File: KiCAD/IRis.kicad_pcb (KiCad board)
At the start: 2 copper layers, 31.3 x 31.3 mm, 25 parts, among them P1 Digital Out, Q1 MMBF4117, Q2 MMBF4117, Q3 MMBF4117, U1 TSV911ILT, U2 TLV3201

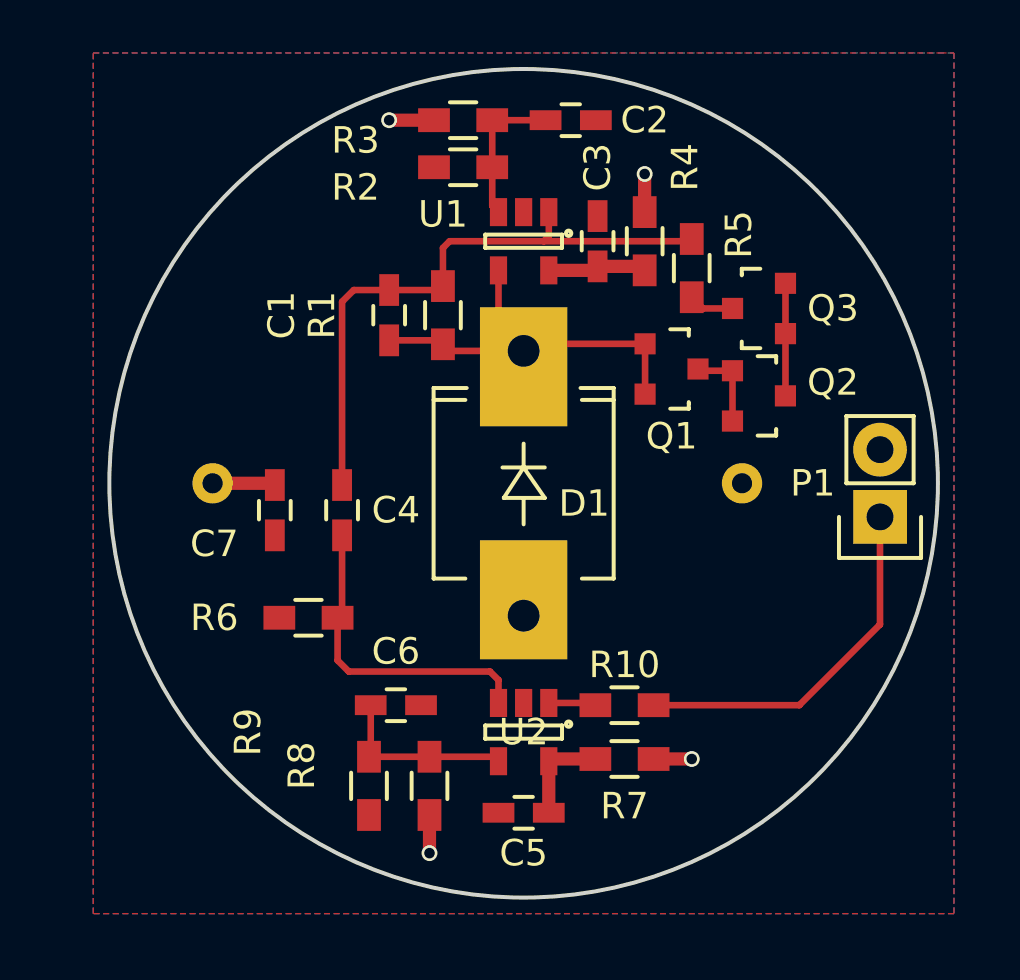
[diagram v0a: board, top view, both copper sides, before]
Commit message: Added negative voltage input protection to comparator U2; fixed copper fill clearances for OSHPark
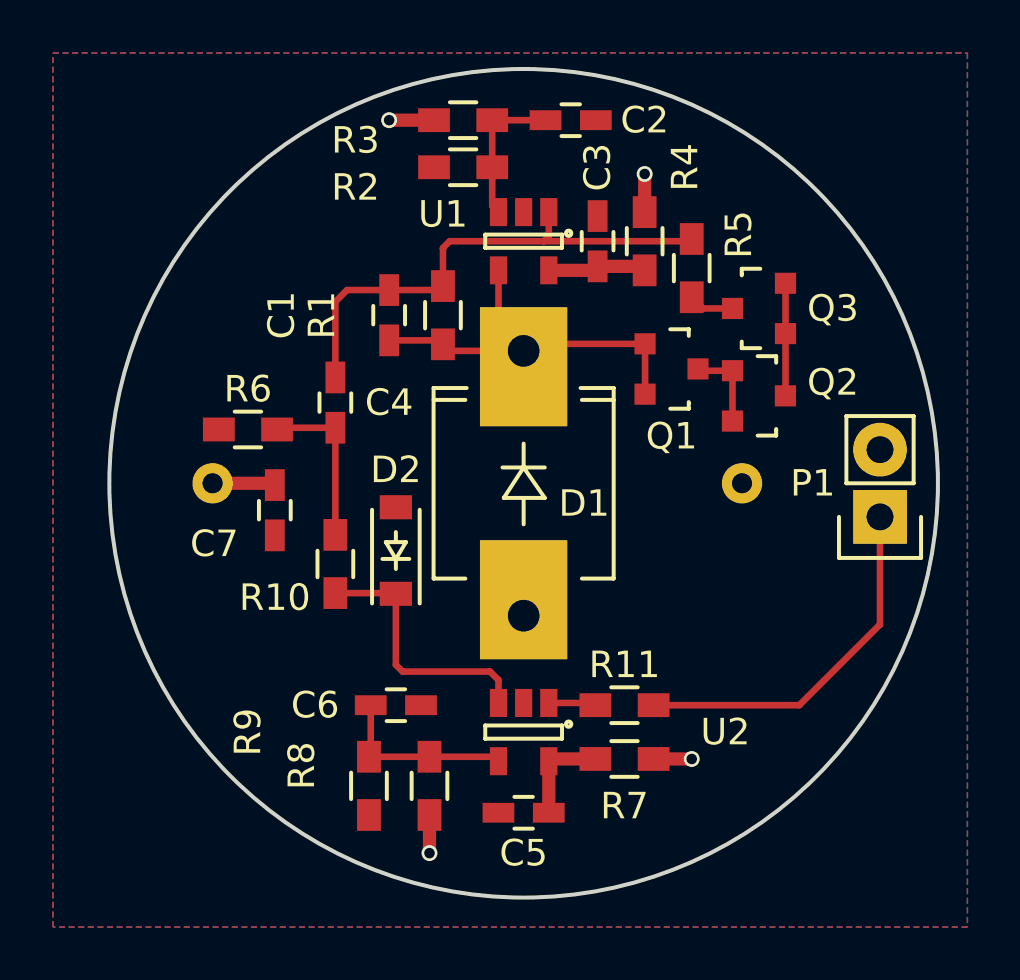
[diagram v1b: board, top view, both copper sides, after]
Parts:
- added D2: MBR0520, Diodes_SMD:SOD-123, F.Cu at (137.4, 102.1)
- added R11: 100, Resistors_SMD:R_0603_HandSoldering, F.Cu at (146.1, 108.0)
- D1: value PD70-01C/TR7 -> VBPW34FASR
- R10: value 100 -> 5.1k
- R6: value 10k -> 5.1k
- moved R10 12.2 mm to (135.1, 102.6), turned to 270 degrees
- moved R6 7.47 mm to (131.8, 97.5)
- moved C4 4.07 mm to (135.1, 96.5)
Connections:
- R10 pad 1: Net-(R10-Pad1) -> Net-(C4-Pad1)
- R10 pad 2: Net-(P1-Pad1) -> Net-(D2-Pad1)
- U2 pad 1: Net-(R10-Pad1) -> Net-(R11-Pad1)
- U2 pad 3: Net-(C4-Pad1) -> Net-(D2-Pad1)
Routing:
- net Net-(D2-Pad1): track 0.00 -> 9.96 mm
- net Net-(C4-Pad1): track 12.0 -> 6.28 mm
- net Net-(C1-Pad1): track 23.5 -> 19.6 mm
- net Net-(R11-Pad1): track 0.00 -> 2.03 mm
- net Net-(R10-Pad1): track 1.91 -> 0.00 mm

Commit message: Updated board and Gerbers to v1.4
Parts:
- moved R11 4.06 mm to (150.1, 108.0)
- moved R6 1.44 mm to (132.8, 96.5), turned to 270 degrees
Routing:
- net Net-(R11-Pad1): track 2.03 -> 5.98 mm
- net Net-(P1-Pad1): track 13.9 -> 9.96 mm
- net +5V: track 8.58 -> 10.1 mm
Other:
- board text added: "IRis v1.4"
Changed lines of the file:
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@@
     (links 48)
     (no_connects 0)
-    (area 124.46 82.827 160.048429 116.332001)
+    (area 126.51563 83.84363 157.96437 115.29237)
     (thickness 1.6)
-    (drawings 1)
-    (tracks 78)
+    (drawings 2)
+    (tracks 81)
     (zones 0)
     (modules 27)
@@
   )
   (setup
-    (last_trace_width 0.25)
+    (last_trace_width 0.5)
     (user_trace_width 0.5)
     (trace_clearance 0.2)
@@
     (tags "capacitor 0603")
     (attr smd)
-    (fp_text reference C1 (at 0 4.064 270) (layer F.SilkS)
+    (fp_text reference C1 (at -0.762 4.572 270) (layer F.SilkS)
       (effects (font (size 1 1) (thickness 0.15)))
     )
@@
     (tags "capacitor 0603")
     (attr smd)
-    (fp_text reference C4 (at 0 2.032 180) (layer F.SilkS)
+    (fp_text reference C4 (at 0 1.524 270) (layer F.SilkS)
       (effects (font (size 1 1) (thickness 0.15)))
     )
@@
     (tags "resistor 0603")
     (attr smd)
-    (fp_text reference R1 (at 0 4.572 270) (layer F.SilkS)
+    (fp_text reference R1 (at -0.762 5.334 270) (layer F.SilkS)
       (effects (font (size 1 1) (thickness 0.15)))
     )
@@
   )
   (module Resistors_SMD:R_0603_HandSoldering (layer F.Cu)
-    (at 131.826 97.536)
-    (descr "Resistor SMD 0603, hand soldering")
-    (tags "resistor 0603")
-    (attr smd)
-    (fp_text reference R6 (at 0 -1.524) (layer F.SilkS)
-      (effects (font (size 1 1) (thickness 0.15)))
-    )
-    (fp_text value 5.1k (at 0 1.9) (layer F.Fab)
-      (effects (font (size 1 1) (thickness 0.15)))
-    )
-    (fp_line (start -2 -0.8) (end 2 -0.8) (layer F.CrtYd) (width 0.05))
-    (fp_line (start -2 0.8) (end 2 0.8) (layer F.CrtYd) (width 0.05))
-    (fp_line (start -2 -0.8) (end -2 0.8) (layer F.CrtYd) (width 0.05))
-    (fp_line (start 2 -0.8) (end 2 0.8) (layer F.CrtYd) (width 0.05))
-    (fp_line (start 0.5 0.675) (end -0.5 0.675) (layer F.SilkS) (width 0.15))
-    (fp_line (start -0.5 -0.675) (end 0.5 -0.675) (layer F.SilkS) (width 0.15))
-    (pad 1 smd rect (at -1.1 0) (size 1.2 0.9) (layers F.Cu F.Paste F.Mask)
-      (net 4 GND))
-    (pad 2 smd rect (at 1.1 0) (size 1.2 0.9) (layers F.Cu F.Paste F.Mask)
+    (at 132.842 96.52 270)
+    (descr "Resistor SMD 0603, hand soldering")
+    (tags "resistor 0603")
+    (attr smd)
+    (fp_text reference R6 (at 0 1.524 270) (layer F.SilkS)
+      (effects (font (size 1 1) (thickness 0.15)))
+    )
+    (fp_text value 5.1k (at 0 1.9 270) (layer F.Fab)
+      (effects (font (size 1 1) (thickness 0.15)))
+    )
+    (fp_line (start -2 -0.8) (end 2 -0.8) (layer F.CrtYd) (width 0.05))
+    (fp_line (start -2 0.8) (end 2 0.8) (layer F.CrtYd) (width 0.05))
+    (fp_line (start -2 -0.8) (end -2 0.8) (layer F.CrtYd) (width 0.05))
+    (fp_line (start 2 -0.8) (end 2 0.8) (layer F.CrtYd) (width 0.05))
+    (fp_line (start 0.5 0.675) (end -0.5 0.675) (layer F.SilkS) (width 0.15))
+    (fp_line (start -0.5 -0.675) (end 0.5 -0.675) (layer F.SilkS) (width 0.15))
+    (pad 1 smd rect (at -1.1 0 270) (size 1.2 0.9) (layers F.Cu F.Paste F.Mask)
+      (net 4 GND))
+    (pad 2 smd rect (at 1.1 0 270) (size 1.2 0.9) (layers F.Cu F.Paste F.Mask)
       (net 6 "Net-(C4-Pad1)"))
     (model Resistors_SMD.3dshapes/R_0603_HandSoldering.wrl
@@
     (tags SOT-23-5)
     (attr smd)
-    (fp_text reference U2 (at 0 -7.62 360) (layer F.SilkS)
+    (fp_text reference U2 (at -1.016 -2.794 360) (layer F.SilkS)
       (effects (font (size 1 1) (thickness 0.15)))
     )
@@
   )
   (module Resistors_SMD:R_0603_HandSoldering (layer F.Cu)
-    (at 146.05 107.95)
+    (at 150.114 107.95)
     (descr "Resistor SMD 0603, hand soldering")
     (tags "resistor 0603")
@@
       (rotate (xyz 0 0 0))
     )
+  )
+  (gr_text "IRis v1.4" (at 149.606 102.616) (layer F.SilkS)
+    (effects (font (size 1 1) (thickness 0.25)))
   )
   (gr_circle (center 142.24 99.568) (end 154.94 108.712) (layer Edge.Cuts) (width 0.15))
@@
   (segment (start 144.884 91.524) (end 145.034 91.374) (width 0.5) (layer F.Cu) (net 5))
   (segment (start 143.34 91.374) (end 143.19 91.524) (width 0.25) (layer F.Cu) (net 5))
+  (segment (start 135.128 97.47) (end 132.992 97.47) (width 0.25) (layer F.Cu) (net 6))
+  (segment (start 132.992 97.47) (end 132.842 97.62) (width 0.25) (layer F.Cu) (net 6))
   (segment (start 135.128 97.47) (end 135.128 101.516) (width 0.25) (layer F.Cu) (net 6))
-  (segment (start 135.128 97.47) (end 132.992 97.47) (width 0.25) (layer F.Cu) (net 6))
-  (segment (start 132.992 97.47) (end 132.926 97.536) (width 0.25) (layer F.Cu) (net 6))
   (segment (start 143.19 110.066) (end 143.19 112.014) (width 0.5) (layer F.Cu) (net 7))
   (segment (start 144.95 109.982) (end 143.274 109.982) (width 0.5) (layer F.Cu) (net 7))
@@
   (segment (start 136.464 107.95) (end 136.464 109.832) (width 0.25) (layer F.Cu) (net 8))
   (segment (start 136.464 109.832) (end 136.398 109.898) (width 0.25) (layer F.Cu) (net 8))
+  (segment (start 138.854 85.852) (end 137.668 85.852) (width 0.5) (layer F.Cu) (net 9))
+  (via (at 137.414 86.868) (size 0.6) (drill 0.4) (layers F.Cu B.Cu) (net 9))
+  (segment (start 137.414 86.106) (end 137.414 86.868) (width 0.5) (layer F.Cu) (net 9))
+  (segment (start 137.668 85.852) (end 137.414 86.106) (width 0.5) (layer F.Cu) (net 9))
+  (segment (start 138.684 112.098) (end 138.684 113.03) (width 0.5) (layer F.Cu) (net 9))
+  (via (at 139.954 113.284) (size 0.6) (drill 0.4) (layers F.Cu B.Cu) (net 9))
+  (segment (start 138.938 113.284) (end 139.954 113.284) (width 0.5) (layer F.Cu) (net 9))
+  (segment (start 138.684 113.03) (end 138.938 113.284) (width 0.5) (layer F.Cu) (net 9))
   (segment (start 130.49 99.568) (end 132.776 99.568) (width 0.5) (layer F.Cu) (net 9))
   (segment (start 132.776 99.568) (end 132.842 99.634) (width 0.5) (layer F.Cu) (net 9))
   (segment (start 147.15 109.982) (end 148.59 109.982) (width 0.5) (layer F.Cu) (net 9))
   (via (at 148.59 109.982) (size 0.6) (drill 0.4) (layers F.Cu B.Cu) (net 9))
-  (segment (start 138.684 112.098) (end 138.684 113.538) (width 0.5) (layer F.Cu) (net 9))
-  (via (at 138.684 113.538) (size 0.6) (drill 0.4) (layers F.Cu B.Cu) (net 9))
   (via (at 146.812 87.884) (size 0.6) (drill 0.4) (layers F.Cu B.Cu) (net 9))
   (segment (start 146.812 89.324) (end 146.812 87.884) (width 0.5) (layer F.Cu) (net 9))
-  (segment (start 138.854 85.852) (end 137.16 85.852) (width 0.5) (layer F.Cu) (net 9))
-  (via (at 137.16 85.852) (size 0.6) (drill 0.4) (layers F.Cu B.Cu) (net 9))
   (segment (start 130.556 99.634) (end 130.49 99.568) (width 0.25) (layer F.Cu) (net 9))
   (segment (start 132.908 99.568) (end 132.842 99.634) (width 0.25) (layer F.Cu) (net 9))
@@
   (segment (start 148.89222 95.316) (end 148.82622 95.25) (width 0.25) (layer F.Cu) (net 10))
   (segment (start 150.12924 97.216) (end 150.12924 95.316) (width 0.25) (layer F.Cu) (net 10))
-  (segment (start 147.15 107.95) (end 152.654 107.95) (width 0.25) (layer F.Cu) (net 11))
-  (segment (start 155.702 104.902) (end 155.702 100.838) (width 0.25) (layer F.Cu) (net 11))
-  (segment (start 152.654 107.95) (end 155.702 104.902) (width 0.25) (layer F.Cu) (net 11))
+  (segment (start 151.214 107.95) (end 152.908 107.95) (width 0.25) (layer F.Cu) (net 11))
+  (segment (start 155.702 105.156) (end 155.702 100.838) (width 0.25) (layer F.Cu) (net 11))
+  (segment (start 152.908 107.95) (end 155.702 105.156) (width 0.25) (layer F.Cu) (net 11))
   (segment (start 152.13076 93.914) (end 152.13076 96.26346) (width 0.25) (layer F.Cu) (net 12))
   (segment (start 152.13076 96.26346) (end 152.12822 96.266) (width 0.25) (layer F.Cu) (net 12))
@@
   (segment (start 135.128 103.716) (end 137.387 103.716) (width 0.25) (layer F.Cu) (net 14))
   (segment (start 137.387 103.716) (end 137.414 103.743) (width 0.25) (layer F.Cu) (net 14))
-  (segment (start 143.19 107.866) (end 144.866 107.866) (width 0.25) (layer F.Cu) (net 15))
-  (segment (start 144.866 107.866) (end 144.95 107.95) (width 0.25) (layer F.Cu) (net 15))
-  (segment (start 144.866 107.866) (end 144.95 107.95) (width 0.25) (layer F.Cu) (net 15))
+  (segment (start 143.19 107.866) (end 148.93 107.866) (width 0.25) (layer F.Cu) (net 15))
+  (segment (start 148.93 107.866) (end 149.014 107.95) (width 0.25) (layer F.Cu) (net 15))
   (segment (start 143.274 107.95) (end 143.19 107.866) (width 0.25) (layer F.Cu) (net 15))
   (zone (net 4) (net_name GND) (layer F.Cu) (hatch edge 0.508)

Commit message: Added external hysteresis to comparator
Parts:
- added R12: 680k, Resistors_SMD:R_0603_HandSoldering, F.Cu at (147.9, 106.1)
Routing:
- net Net-(D2-Pad1): track 9.96 -> 16.7 mm
- net Net-(R11-Pad1): track 5.98 -> 7.86 mm
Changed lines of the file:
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@@
 (kicad_pcb (version 4) (host pcbnew 4.0.2-stable)
   (general
-    (links 48)
+    (links 50)
     (no_connects 0)
-    (area 126.51563 83.84363 157.96437 115.29237)
+    (area 124.46 82.827 160.048429 116.332001)
     (thickness 1.6)
     (drawings 2)
-    (tracks 81)
+    (tracks 90)
     (zones 0)
-    (modules 27)
+    (modules 28)
     (nets 16)
   )
@@
   )
   (setup
-    (last_trace_width 0.5)
+    (last_trace_width 0.25)
     (user_trace_width 0.5)
     (trace_clearance 0.2)
@@
     (tags "resistor 0603")
     (attr smd)
-    (fp_text reference R11 (at 0 -1.524) (layer F.SilkS)
+    (fp_text reference R11 (at 0.7874 1.6764) (layer F.SilkS)
       (effects (font (size 1 1) (thickness 0.15)))
     )
@@
     (pad 2 smd rect (at 1.1 0) (size 1.2 0.9) (layers F.Cu F.Paste F.Mask)
       (net 11 "Net-(P1-Pad1)"))
+    (model Resistors_SMD.3dshapes/R_0603_HandSoldering.wrl
+      (at (xyz 0 0 0))
+      (scale (xyz 1 1 1))
+      (rotate (xyz 0 0 0))
+    )
+  )
+  (module Resistors_SMD:R_0603_HandSoldering (layer F.Cu)
+    (at 147.9042 106.0958 180)
+    (descr "Resistor SMD 0603, hand soldering")
+    (tags "resistor 0603")
+    (attr smd)
+    (fp_text reference R12 (at -3.6068 0 180) (layer F.SilkS)
+      (effects (font (size 1 1) (thickness 0.15)))
+    )
+    (fp_text value 680k (at 0 1.9 180) (layer F.Fab)
+      (effects (font (size 1 1) (thickness 0.15)))
+    )
+    (fp_line (start -2 -0.8) (end 2 -0.8) (layer F.CrtYd) (width 0.05))
+    (fp_line (start -2 0.8) (end 2 0.8) (layer F.CrtYd) (width 0.05))
+    (fp_line (start -2 -0.8) (end -2 0.8) (layer F.CrtYd) (width 0.05))
+    (fp_line (start 2 -0.8) (end 2 0.8) (layer F.CrtYd) (width 0.05))
+    (fp_line (start 0.5 0.675) (end -0.5 0.675) (layer F.SilkS) (width 0.15))
+    (fp_line (start -0.5 -0.675) (end 0.5 -0.675) (layer F.SilkS) (width 0.15))
+    (pad 1 smd rect (at -1.1 0 180) (size 1.2 0.9) (layers F.Cu F.Paste F.Mask)
+      (net 15 "Net-(R11-Pad1)"))
+    (pad 2 smd rect (at 1.1 0 180) (size 1.2 0.9) (layers F.Cu F.Paste F.Mask)
+      (net 14 "Net-(D2-Pad1)"))
     (model Resistors_SMD.3dshapes/R_0603_HandSoldering.wrl
       (at (xyz 0 0 0))
@@
   (segment (start 150.13178 92.964) (end 149.014 92.964) (width 0.25) (layer F.Cu) (net 13))
   (segment (start 149.014 92.964) (end 148.59 92.54) (width 0.25) (layer F.Cu) (net 13))
+  (segment (start 146.8042 106.0958) (end 146.8042 106.3576) (width 0.25) (layer F.Cu) (net 14))
+  (segment (start 146.8042 106.3576) (end 146.4818 106.68) (width 0.25) (layer F.Cu) (net 14))
+  (segment (start 146.4818 106.68) (end 140.97 106.68) (width 0.25) (layer F.Cu) (net 14))
+  (segment (start 146.8042 106.2736) (end 146.5326 106.2736) (width 0.25) (layer F.Cu) (net 14))
+  (segment (start 146.8042 106.1212) (end 146.8042 106.3322) (width 0.25) (layer F.Cu) (net 14))
   (segment (start 137.414 103.743) (end 137.414 106.426) (width 0.25) (layer F.Cu) (net 14))
   (segment (start 141.29 107) (end 141.29 107.866) (width 0.25) (layer F.Cu) (net 14))
@@
   (segment (start 135.128 103.716) (end 137.387 103.716) (width 0.25) (layer F.Cu) (net 14))
   (segment (start 137.387 103.716) (end 137.414 103.743) (width 0.25) (layer F.Cu) (net 14))
+  (segment (start 149.0042 106.0958) (end 149.0042 107.9402) (width 0.25) (layer F.Cu) (net 15))
+  (segment (start 149.0042 107.9402) (end 149.014 107.95) (width 0.25) (layer F.Cu) (net 15))
+  (segment (start 149.0042 107.9402) (end 149.014 107.95) (width 0.5) (layer F.Cu) (net 15))
+  (segment (start 149.0042 107.9402) (end 149.014 107.95) (width 0.25) (layer F.Cu) (net 15))
   (segment (start 143.19 107.866) (end 148.93 107.866) (width 0.25) (layer F.Cu) (net 15))
   (segment (start 148.93 107.866) (end 149.014 107.95) (width 0.25) (layer F.Cu) (net 15))

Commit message: Added ground icon to P1 silkscreen; rotated P1 180 degrees.
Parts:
- moved P1 2.30 mm to (155.4, 98.6), turned to 0 degrees
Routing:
- net Net-(P1-Pad1): track 9.96 -> 13.2 mm
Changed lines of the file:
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@@
     (links 50)
     (no_connects 0)
-    (area 124.46 82.827 160.048429 116.332001)
+    (area 124.46 82.827 159.794429 116.332001)
     (thickness 1.6)
-    (drawings 2)
-    (tracks 90)
+    (drawings 10)
+    (tracks 92)
     (zones 0)
     (modules 28)
@@
   )
   (module Pin_Headers:Pin_Header_Straight_1x02 (layer F.Cu)
-    (at 155.702 100.838 180)
+    (at 155.448 98.552)
     (descr "Through hole pin header")
     (tags "pin header")
-    (fp_text reference P1 (at 2.54 1.27 360) (layer F.SilkS)
-      (effects (font (size 1 1) (thickness 0.15)))
-    )
-    (fp_text value "Digital Out" (at 0 -3.1 180) (layer F.Fab)
+    (fp_text reference P1 (at -2.54 1.27 180) (layer F.SilkS)
+      (effects (font (size 1 1) (thickness 0.15)))
+    )
+    (fp_text value "Digital Out" (at 0 -3.1) (layer F.Fab)
       (effects (font (size 1 1) (thickness 0.15)))
     )
@@
     (fp_line (start -1.27 1.27) (end -1.27 3.81) (layer F.SilkS) (width 0.15))
     (fp_line (start -1.27 3.81) (end 1.27 3.81) (layer F.SilkS) (width 0.15))
-    (pad 1 thru_hole rect (at 0 0 180) (size 2.032 2.032) (drill 1.016) (layers *.Cu *.Mask F.SilkS)
+    (pad 1 thru_hole rect (at 0 0) (size 2.032 2.032) (drill 1.016) (layers *.Cu *.Mask F.SilkS)
       (net 11 "Net-(P1-Pad1)"))
-    (pad 2 thru_hole oval (at 0 2.54 180) (size 2.032 2.032) (drill 1.016) (layers *.Cu *.Mask F.SilkS)
+    (pad 2 thru_hole oval (at 0 2.54) (size 2.032 2.032) (drill 1.016) (layers *.Cu *.Mask F.SilkS)
       (net 4 GND))
     (model Pin_Headers.3dshapes/Pin_Header_Straight_1x02.wrl
@@
     )
   )
+  (gr_line (start 155.194 104.394) (end 155.702 104.394) (angle 90) (layer F.SilkS) (width 0.2))
+  (gr_line (start 155.448 104.394) (end 155.194 104.394) (angle 90) (layer F.SilkS) (width 0.2))
+  (gr_line (start 154.686 103.886) (end 156.21 103.886) (angle 90) (layer F.SilkS) (width 0.2))
+  (gr_line (start 155.448 103.886) (end 154.686 103.886) (angle 90) (layer F.SilkS) (width 0.2))
+  (gr_line (start 156.718 103.378) (end 154.178 103.378) (angle 90) (layer F.SilkS) (width 0.2))
+  (gr_line (start 154.432 103.378) (end 156.718 103.378) (angle 90) (layer F.SilkS) (width 0.2))
+  (gr_line (start 155.448 103.378) (end 154.432 103.378) (angle 90) (layer F.SilkS) (width 0.2))
+  (gr_line (start 155.448 102.362) (end 155.448 103.378) (angle 90) (layer F.SilkS) (width 0.2))
   (gr_text "IRis v1.4" (at 149.606 102.616) (layer F.SilkS)
     (effects (font (size 1 1) (thickness 0.25)))
@@
   (segment (start 150.12924 97.216) (end 150.12924 95.316) (width 0.25) (layer F.Cu) (net 10))
   (segment (start 151.214 107.95) (end 152.908 107.95) (width 0.25) (layer F.Cu) (net 11))
-  (segment (start 155.702 105.156) (end 155.702 100.838) (width 0.25) (layer F.Cu) (net 11))
-  (segment (start 152.908 107.95) (end 155.702 105.156) (width 0.25) (layer F.Cu) (net 11))
+  (segment (start 153.67 98.552) (end 155.448 98.552) (width 0.25) (layer F.Cu) (net 11))
+  (segment (start 153.416 98.806) (end 153.67 98.552) (width 0.25) (layer F.Cu) (net 11))
+  (segment (start 153.416 107.442) (end 153.416 98.806) (width 0.25) (layer F.Cu) (net 11))
+  (segment (start 152.908 107.95) (end 153.416 107.442) (width 0.25) (layer F.Cu) (net 11))
   (segment (start 152.13076 93.914) (end 152.13076 96.26346) (width 0.25) (layer F.Cu) (net 12))
   (segment (start 152.13076 96.26346) (end 152.12822 96.266) (width 0.25) (layer F.Cu) (net 12))
